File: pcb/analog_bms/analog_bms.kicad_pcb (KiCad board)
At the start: 4 copper layers, 42 x 22 mm, 45 parts, among them J1 Screw_Terminal_1x2, J2 MODULE+, J3 MODULE-, Q1 PMOS, Q2 NMOS, Q3 PMOS, Q4 NMOS, Q5 PMOS, U1 TLV7031DBV, U2 TLV7031DBV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

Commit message: CAD Model
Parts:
- moved J2 0.50 mm to (134.5, 123.5)
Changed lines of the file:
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@@
 	(footprint "TestPoint:TestPoint_THTPad_D3.0mm_Drill1.5mm"
 		(layer "F.Cu")
-		(at 134.5 123 90)
+		(at 134.5 123.5 90)
 		(descr "THT pad as test Point, diameter 3.0mm, hole diameter 1.5mm")
 		(tags "test point THT pad")

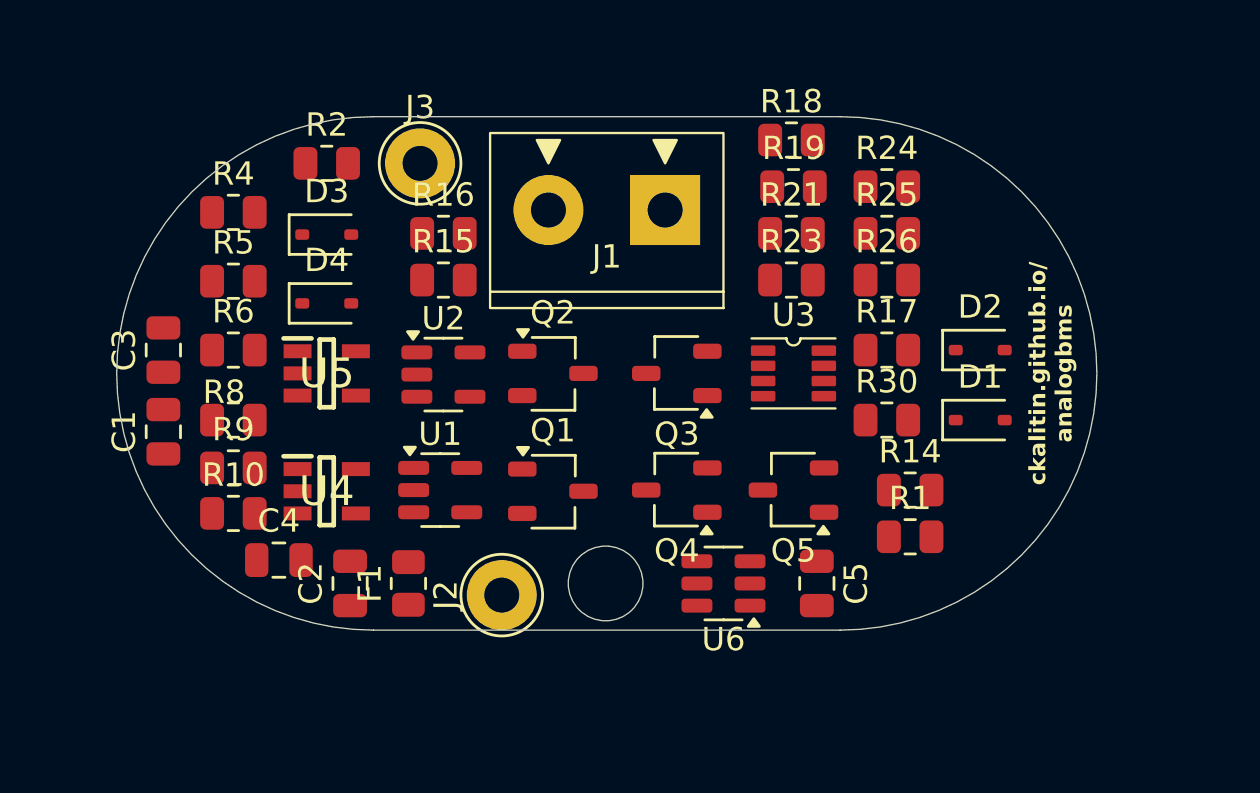
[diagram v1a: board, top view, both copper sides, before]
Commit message: PCB Design Complete - Pass DRC
Still skeptical of the DRC. Some very close silk screen elements.
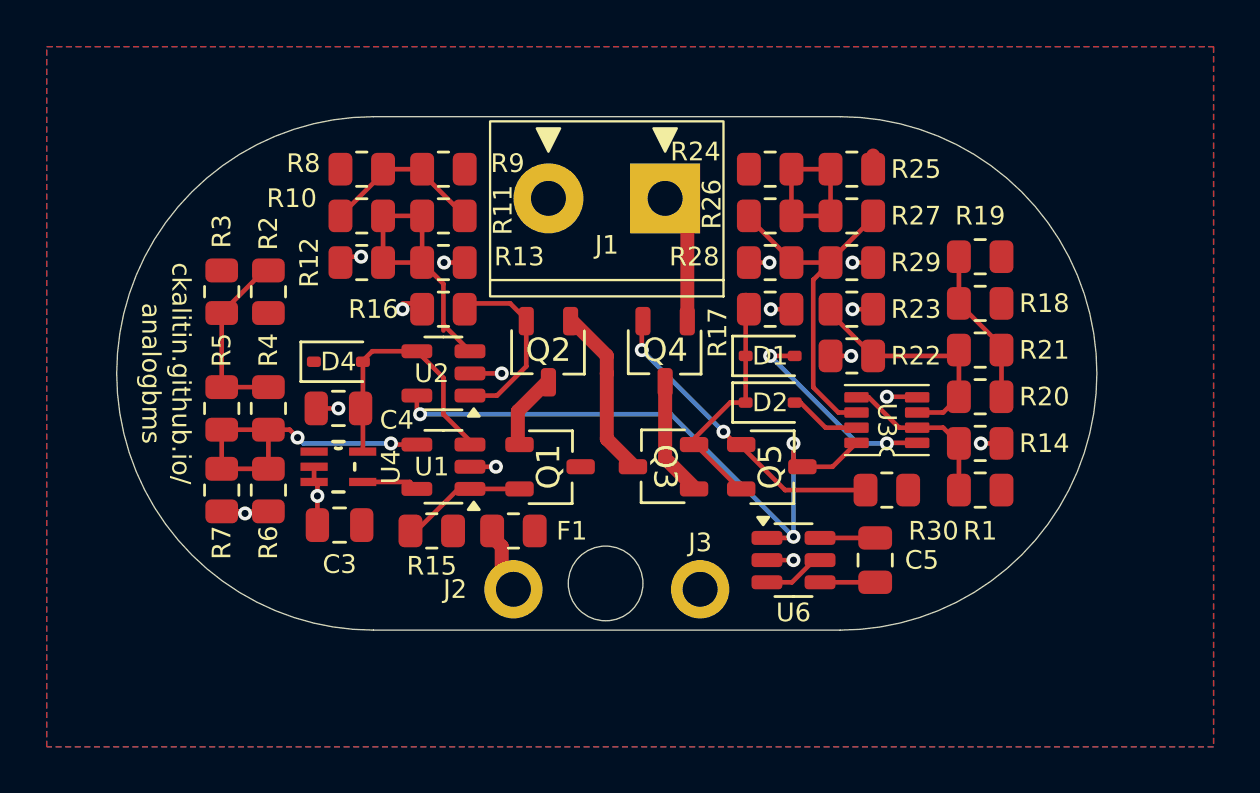
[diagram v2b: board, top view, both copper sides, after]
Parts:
- removed C1: 2u2, Capacitor_SMD:C_0805_2012Metric
- removed C2: 1u, Capacitor_SMD:C_0805_2012Metric
- removed D3: D_Schottky, Diode_SMD:D_SOD-323
- removed U5: TPS7A2401DBVR, analog_bms_library:SOT95P280X145-5N
- added R11: 100, Resistor_SMD:R_0805_2012Metric, F.Cu at (132.0, 107.2)
- added R12: R, Resistor_SMD:R_0805_2012Metric, F.Cu at (128.5, 109.2)
- added R13: 1M, Resistor_SMD:R_0805_2012Metric, F.Cu at (132.0, 109.2)
- added R20: R, Resistor_SMD:R_0805_2012Metric, F.Cu at (155.0, 115.0)
- added R22: R, Resistor_SMD:R_0805_2012Metric, F.Cu at (149.5, 113.2)
- added R25: R, Resistor_SMD:R_0805_2012Metric, F.Cu at (149.5, 105.2)
- added R27: R, Resistor_SMD:R_0805_2012Metric, F.Cu at (149.5, 107.2)
- added R29: R, Resistor_SMD:R_0805_2012Metric, F.Cu at (149.5, 109.2)
- added R3: 1M, Resistor_SMD:R_0805_2012Metric, F.Cu at (122.5, 110.5)
- added R7: 1M, Resistor_SMD:R_0805_2012Metric, F.Cu at (122.5, 119.0)
- C4: value 2u2 -> 1u
- J2, J3: footprint TestPoint:TestPoint_THTPad_D3.0mm_Drill1.5mm -> analog_bms_library:1.5_mm_Through_Hole
- Q1, Q2, Q3, Q4, Q5: footprint Package_TO_SOT_SMD:TSOT-23 -> analog_bms_library:TSOT_23_No_Arrow
- R10: value 470k -> R
- R4: value 100k -> R
- R5: value 100k -> 100
- R6: value 1M -> R
- R9: value 100k -> 1M
- U4: value TPS7A2401DBVR -> TPS71518DCKRM3; footprint analog_bms_library:SOT95P280X145-5N -> analog_bms_library:TPS71518DCKRM3
- moved J3 21.8 mm to (143.0, 123.2)
- moved R9 15.6 mm to (132.0, 105.2), turned to 180 degrees
- moved R10 13.9 mm to (128.5, 107.2)
- moved R8 12.1 mm to (128.5, 105.2)
- moved R15 10.8 mm to (131.5, 120.8)
- moved R18 10.7 mm to (155.0, 111.0), turned to 180 degrees
- moved C3 10.6 mm to (127.5, 120.5), turned to 180 degrees
- moved R21 9.51 mm to (155.0, 113.0), turned to 180 degrees
- moved D1 9.41 mm to (146.0, 113.2)
- moved D2 9.28 mm to (146.0, 115.2)
- moved R19 8.54 mm to (155.0, 109.0), turned to 180 degrees
- moved R4 8.53 mm to (124.5, 115.5), turned to -90 degrees
- moved C4 6.98 mm to (127.5, 115.5), turned to 180 degrees
- moved R6 6.18 mm to (124.5, 119.0), turned to -90 degrees
- moved R2 6.04 mm to (124.5, 110.5), turned to 90 degrees
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- renumbered R25 to R26, R26 to R28
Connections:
- R10 pad 1: Net-(U5-FB) -> Net-(R10-Pad1)
- R10 pad 2: -MODULE -> Net-(U2-+)
- R2 pad 1: Net-(D3-A) -> +BATT
- R4 pad 2: Net-(U4-FB) -> Net-(U1--)
- R5 pad 2: Net-(U4-FB) -> Net-(U1--)
- R6 pad 1: Net-(U4-FB) -> Net-(U1--)
- R8 pad 1: Net-(D4-A) -> +BATT
- R8 pad 2: Net-(R8-Pad2) -> Net-(R10-Pad1)
- R9 pad 1: Net-(R8-Pad2) -> +BATT
- R9 pad 2: Net-(U5-FB) -> Net-(R10-Pad1)
- U1 pad 3: Net-(D3-A) -> Net-(D4-A)
- U1 pad 4: +BATT -> Net-(U1--)
- U2 pad 3: +BATT -> Net-(U2-+)
- U4 pad 1: +BATT -> unconnected-(U4-FB/NC-Pad1)
- U4 pad 3: +BATT -> -MODULE
- U4 pad 4: Net-(U4-FB) -> +BATT
- U4 pad 5: Net-(D3-A) -> Net-(D4-A)
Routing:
- net +5V: track 0.00 -> 28.2 mm, vias 0 -> 3
- net -MODULE: track 0.00 -> 18.7 mm, vias 0 -> 16
- net Net-(U3-INB-): track 0.00 -> 15.1 mm
- net Net-(U1--): track 0.00 -> 14.0 mm, vias 0 -> 2
- net Net-(Q4-G): track 0.00 -> 13.4 mm, vias 0 -> 2
- net Net-(U2-+): track 0.00 -> 12.2 mm
- net Net-(D4-A): track 0.00 -> 11.3 mm
- net Net-(U3-INA+): track 0.00 -> 10.7 mm
- net Net-(D1-K): track 0.00 -> 10.4 mm
- net Net-(D1-A): track 0.00 -> 8.91 mm, vias 0 -> 2
- net Net-(R2-Pad2): track 0.00 -> 7.93 mm
- net Net-(Q2-G): track 0.00 -> 7.79 mm
- net Net-(Q2-D): track 0.00 -> 7.44 mm
- net Net-(R24-Pad2): track 0.00 -> 7.35 mm
- net Net-(R10-Pad1): track 0.00 -> 7.19 mm
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- added copper zone on F.Cu, net +BATT
- added copper zone on B.Cu, net -MODULE
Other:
- copper layers 4 -> 2
- board text added: "Analog BMS rev 1.0 Christopher Kalitin 2025"

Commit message: Black PCB + Renders
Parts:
- moved C5 0.56 mm to (151.0, 121.8)
- moved U6 0.56 mm to (147.5, 121.8)
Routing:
- net +BATT: track 5.71 -> 12.2 mm
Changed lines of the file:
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@@
 			(layer "F.Mask"
 				(type "Top Solder Mask")
+				(color "Black")
 				(thickness 0.01)
 			)
@@
 			(layer "B.Mask"
 				(type "Bottom Solder Mask")
+				(color "Black")
 				(thickness 0.01)
 			)
@@
 	(footprint "Capacitor_SMD:C_0805_2012Metric"
 		(layer "F.Cu")
-		(at 150.5 122 -90)
+		(at 151 121.75 -90)
 		(descr "Capacitor SMD 0805 (2012 Metric), square (rectangular) end terminal, IPC-7351 nominal, (Body size source: IPC-SM-782 page 76, https://www.pcb-3d.com/wordpress/wp-content/uploads/ipc-sm-782a_amendment_1_and_2.pdf, https://docs.google.com/spreadsheets/d/1BsfQQcO9C6DZCsRaXUlFlo91Tg2WpOkGARC1WS5S8t0/edit?usp=sharing), generated with kicad-footprint-generator")
 		(tags "capacitor")
 		(property "Reference" "C5"
-			(at 0 -2 180)
+			(at 0 -1.9 180)
 			(layer "F.SilkS")
 			(effects
@@
 		(tags "resistor")
 		(property "Reference" "R1"
-			(at 0 -1.75 0)
+			(at -0.25 -1.75 0)
 			(layer "F.SilkS")
 			(effects
@@
 	(footprint "Package_TO_SOT_SMD:SOT-23-6"
 		(layer "F.Cu")
-		(at 147 122)
+		(at 147.5 121.75)
 		(descr "SOT, 6 Pin (JEDEC MO-178 Var AB https://www.jedec.org/document_search?search_api_views_fulltext=MO-178), generated with kicad-footprint-generator ipc_gullwing_generator.py")
 		(tags "SOT TO_SOT_SMD")
@@
 		(tags "resistor")
 		(property "Reference" "R30"
-			(at 2 1.75 0)
+			(at 2.25 1.75 0)
 			(layer "F.SilkS")
 			(effects
@@
 	)
 	(segment
-		(start 145.8625 122)
-		(end 147 122)
+		(start 146.3625 121.75)
+		(end 147.5 121.75)
 		(width 0.2)
 		(layer "F.Cu")
@@
 	)
 	(via
-		(at 147 122)
+		(at 147.5 121.75)
 		(size 0.6)
 		(drill 0.3)
@@
 	)
 	(segment
-		(start 147.886272 122)
-		(end 148.1375 122)
-		(width 0.2)
+		(start 155.9125 120.5875)
+		(end 155.9125 119)
+		(width 0.6)
 		(layer "F.Cu")
 		(net 2)
@@
 	)
 	(segment
+		(start 153.8 120.9)
+		(end 155.6 120.9)
+		(width 0.6)
+		(layer "F.Cu")
+		(net 2)
+	)
+	(segment
 		(start 128.5414 118.649999)
 		(end 130.562499 118.649999)
@@
 	)
 	(segment
+		(start 155.6 120.9)
+		(end 155.9125 120.5875)
+		(width 0.6)
+		(layer "F.Cu")
+		(net 2)
+	)
+	(segment
+		(start 147.436272 122.7)
+		(end 148.386272 121.75)
+		(width 0.2)
+		(layer "F.Cu")
+		(net 2)
+	)
+	(segment
+		(start 146.3625 122.7)
+		(end 147.436272 122.7)
+		(width 0.2)
+		(layer "F.Cu")
+		(net 2)
+	)
+	(segment
 		(start 150.4125 105)
 		(end 150.4125 104.6625)
@@
 	)
 	(segment
-		(start 146.936272 122.95)
-		(end 147.886272 122)
+		(start 148.386272 121.75)
+		(end 148.6375 121.75)
 		(width 0.2)
 		(layer "F.Cu")
@@
 	)
 	(segment
-		(start 145.8625 122.95)
-		(end 146.936272 122.95)
-		(width 0.2)
+		(start 151.9125 119.0125)
+		(end 153.8 120.9)
+		(width 0.6)
 		(layer "F.Cu")
 		(net 2)
@@
 	)
 	(segment
+		(start 151.9125 119)
+		(end 151.9125 119.0125)
+		(width 0.6)
+		(layer "F.Cu")
+		(net 2)
+	)
+	(segment
 		(start 127.5875 105)
 		(end 127.5875 104.9125)
@@
 	)
 	(segment
-		(start 148.1375 121.05)
-		(end 150.5 121.05)
+		(start 148.3875 121.05)
+		(end 150.75 121.05)
 		(width 0.2)
 		(layer "F.Cu")
@@
 	)
 	(segment
-		(start 146.95 121.05)
-		(end 147 121)
+		(start 147.25 121)
+		(end 147.2 121.05)
 		(width 0.2)
 		(layer "F.Cu")
@@
 	)
 	(segment
-		(start 147 117)
-		(end 147 117.69)
-		(width 0.2)
+		(start 147.38 118)
+		(end 147.31 118)
+		(width 0.127)
 		(layer "F.Cu")
 		(net 15)
 	)
 	(segment
-		(start 147 117.69)
-		(end 147.31 118)
+		(start 147.2 121.05)
+		(end 146.1125 121.05)
 		(width 0.2)
 		(layer "F.Cu")
@@
 	)
 	(segment
-		(start 145.8625 121.05)
-		(end 146.95 121.05)
+		(start 147.38 117.38)
+		(end 147.25 117.25)
+		(width 0.127)
+		(layer "F.Cu")
+		(net 15)
+	)
+	(segment
+		(start 147.31 118)
+		(end 148.675 118)
 		(width 0.2)
 		(layer "F.Cu")
@@
 	)
 	(segment
-		(start 130.8625 114.95)
-		(end 130.8625 115.6125)
+		(start 148.675 118)
+		(end 149.7 116.975)
 		(width 0.2)
 		(layer "F.Cu")
@@
 	)
 	(segment
-		(start 147.31 118)
-		(end 148.675 118)
+		(start 130.8625 114.95)
+		(end 130.8625 115.6125)
 		(width 0.2)
 		(layer "F.Cu")
@@
 	)
 	(segment
-		(start 148.675 118)
-		(end 149.7 116.975)
-		(width 0.2)
+		(start 147.38 118)
+		(end 147.38 117.38)
+		(width 0.127)
 		(layer "F.Cu")
 		(net 15)
 	)
 	(via
-		(at 147 121)
+		(at 147.25 121)
 		(size 0.6)
 		(drill 0.3)
@@
 	)
 	(via
-		(at 131 115.75)
+		(at 147.25 117.25)
 		(size 0.6)
 		(drill 0.3)
@@
 	)
 	(via
-		(at 147 117)
+		(at 131 115.75)
 		(size 0.6)
 		(drill 0.3)
@@
 	)
 	(segment
-		(start 141.75 115.75)
-		(end 147 121)
+		(start 147.25 121)
+		(end 142 115.75)
 		(width 0.2)
 		(layer "B.Cu")
@@
 	)
 	(segment
-		(start 147 121)
-		(end 147 117)
-		(width 0.2)
+		(start 147.25 117.25)
+		(end 147.25 121)
+		(width 0.127)
 		(layer "B.Cu")
 		(net 15)
 	)
 	(segment
-		(start 131 115.75)
-		(end 141.75 115.75)
-		(width 0.2)
-		(layer "B.Cu")
-		(net 15)
-	)
-	(segment
-		(start 147 117)
-		(end 146.972 117.028)
+		(start 142 115.75)
+		(end 131 115.75)
 		(width 0.2)
 		(layer "B.Cu")

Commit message: pepes heh
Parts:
- added G***: LOGO, LOGO, B.Cu at (147.0, 120.7)
- added G***: LOGO, LOGO, B.Cu at (132.0, 109.2)
- added G***: LOGO, LOGO, B.Cu at (125.0, 116.4)
- added G***: LOGO, LOGO, B.Cu at (152.7, 114.8)

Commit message: + & - silkscreen
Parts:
- moved G*** 3.97 mm to (154.3, 111.2)
- moved G*** 3.46 mm to (150.2, 119.5)
- moved G*** 1.52 mm to (130.5, 109.5)
- moved F1 0.50 mm to (135.5, 120.8)
- moved R15 0.50 mm to (132.0, 120.8)
- turned R23 to 180 degrees
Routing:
- net +5V: track 27.9 -> 26.3 mm
- net Net-(U3-INA+): track 10.7 -> 10.1 mm
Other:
- board text added: "+"
- board text added: "-"

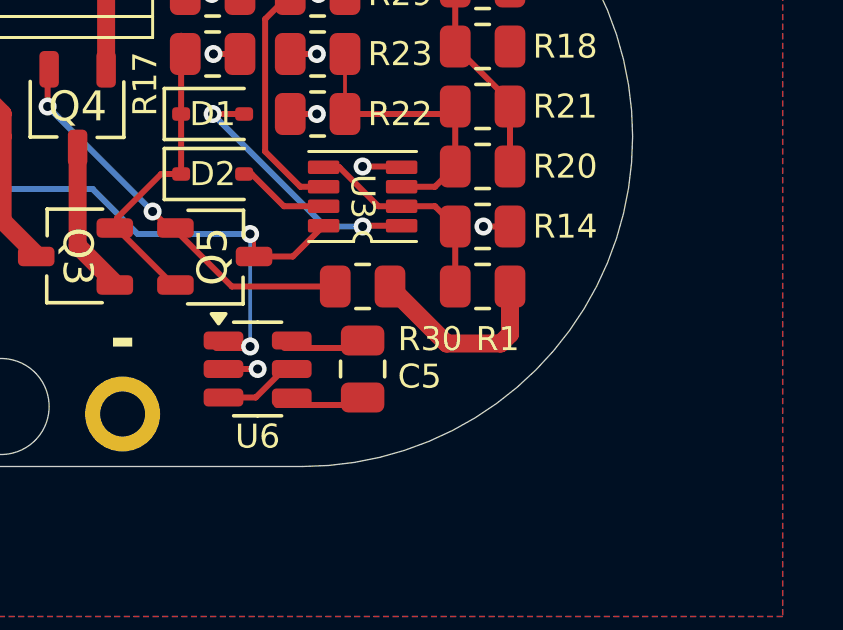
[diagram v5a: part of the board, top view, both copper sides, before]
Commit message: Updated rules & solid connection pours
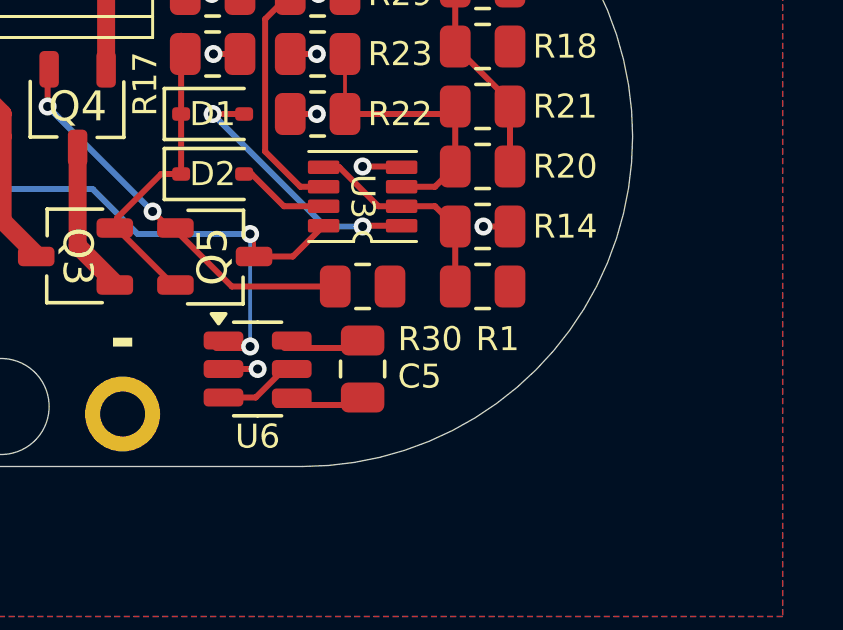
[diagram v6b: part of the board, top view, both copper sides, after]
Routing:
- net +BATT: track 12.2 -> 5.73 mm
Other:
- rule solder_mask_min_width: 0.12 -> 0.1016
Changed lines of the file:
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@@
 	(generator_version "9.0")
 	(general
-		(thickness 1.600198)
+		(thickness 1.6)
 		(legacy_teardrops no)
 	)
 	(paper "A4")
 	(layers
-		(0 "F.Cu" signal "Front")
-		(2 "B.Cu" signal "Back")
+		(0 "F.Cu" signal)
+		(2 "B.Cu" signal)
 		(13 "F.Paste" user)
 		(15 "B.Paste" user)
@@
 		(29 "B.CrtYd" user "B.Courtyard")
 		(35 "F.Fab" user)
+		(33 "B.Fab" user)
 	)
 	(setup
@@
 			(layer "F.Mask"
 				(type "Top Solder Mask")
-				(color "Black")
 				(thickness 0.01)
 			)
@@
 			(layer "dielectric 1"
 				(type "core")
-				(thickness 1.510198)
+				(thickness 1.51)
 				(material "FR4")
 				(epsilon_r 4.5)
@@
 			(layer "B.Mask"
 				(type "Bottom Solder Mask")
-				(color "Black")
 				(thickness 0.01)
 			)
@@
 		)
 		(pad_to_mask_clearance 0)
-		(solder_mask_min_width 0.12)
+		(solder_mask_min_width 0.1016)
 		(allow_soldermask_bridges_in_footprints no)
 		(tenting front back)
@@
 	)
 	(segment
-		(start 155.9125 120.5875)
-		(end 155.9125 119)
-		(width 0.6)
-		(layer "F.Cu")
-		(net 1)
-	)
-	(segment
 		(start 155.9125 111.425)
 		(end 155.9125 111.25)
@@
 	)
 	(segment
-		(start 153.8 120.9)
-		(end 155.6 120.9)
-		(width 0.6)
-		(layer "F.Cu")
-		(net 1)
-	)
-	(segment
 		(start 128.5414 118.649999)
 		(end 130.562499 118.649999)
@@
 	)
 	(segment
-		(start 155.6 120.9)
-		(end 155.9125 120.5875)
-		(width 0.6)
-		(layer "F.Cu")
-		(net 1)
-	)
-	(segment
 		(start 147.436272 122.7)
 		(end 148.386272 121.75)
@@
 	)
 	(segment
-		(start 151.9125 119.0125)
-		(end 153.8 120.9)
-		(width 0.6)
-		(layer "F.Cu")
-		(net 1)
-	)
-	(segment
 		(start 130.562499 118.649999)
 		(end 130.8625 118.95)
@@
 		(layer "F.Cu")
 		(hatch edge 0.5)
-		(connect_pads
+		(connect_pads yes
 			(clearance 0.5)
 		)
@@
 		(hatch edge 0.5)
 		(priority 1)
-		(connect_pads
+		(connect_pads yes
 			(clearance 0.5)
 		)
